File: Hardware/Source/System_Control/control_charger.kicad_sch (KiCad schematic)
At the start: 22 parts, among them Q21 LN2302LT1G, Q22 SQJ211ELP-T1_GE3, Q23 SQJ211ELP-T1_GE3, Q24 LN2302LT1G, U20 EL3H7, U21 EL3H7

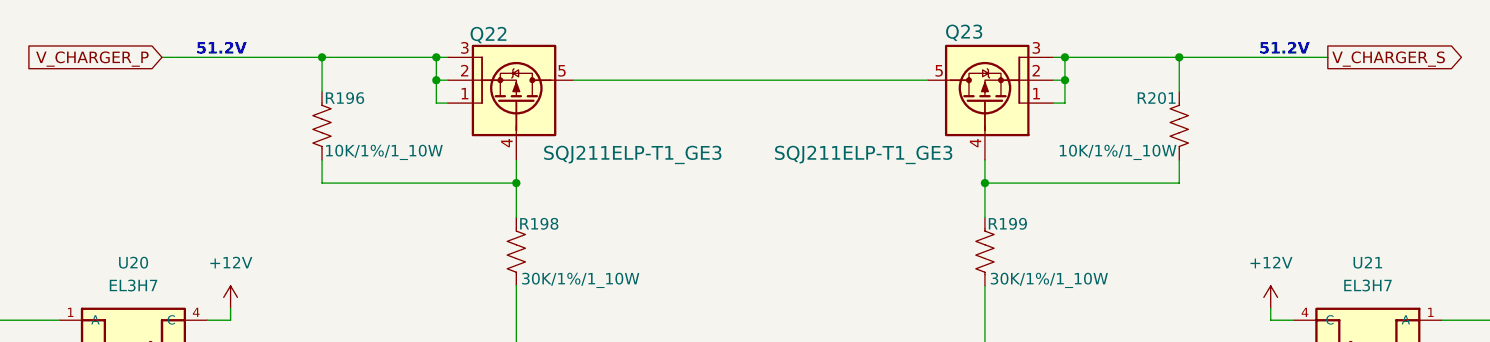
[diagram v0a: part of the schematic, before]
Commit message: schematic: update connector charger board F4
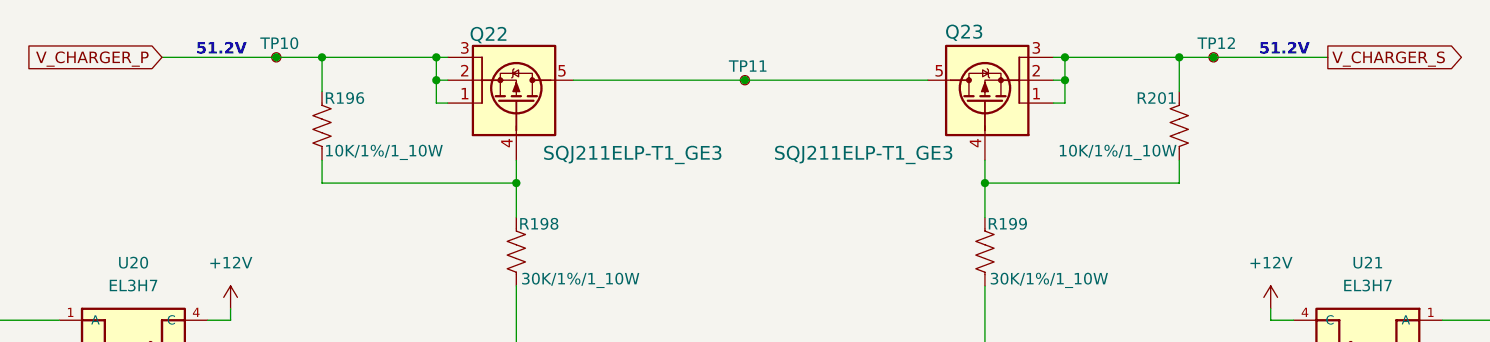
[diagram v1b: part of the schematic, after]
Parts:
- added TP10, TP11, TP12: TestPoint_Small, TestPoint:TestPoint_Pad_D1.0mm, symbol Connector:TestPoint_Small
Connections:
- net V_CHARGER_P: now also TP10.1
- net V_CHARGER_S: now also TP12.1
- net at Q22.5 (D), Q23.5 (D): now also TP11.1

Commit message: pcb,lib,sche: PFC, lib: update pcb PFC, lib
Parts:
- renumbered C164 to C169, C165 to C170, C166 to C171, C167 to C172, D76 to D75, D77 to D76, R194 to R196, R195 to R197, R196 to R198, R197 to R199, R198 to R200, R199 to R201, R200 to R202, R201 to R203, R202 to R204, R203 to R205
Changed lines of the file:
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@@
 		(on_board yes)
 		(dnp no)
-		(property "Reference" "R194"
+		(property "Reference" "R196"
 			(at 53.594 91.948 0)
 			(effects
@@
 			(project "System_Control"
 				(path "/85c53e8c-0403-413d-b6c5-0718d4365b1f/dcdba039-ea40-479a-8e78-13cd4769be17"
-					(reference "R194")
+					(reference "R196")
 					(unit 1)
 				)
@@
 		(on_board yes)
 		(dnp no)
-		(property "Reference" "R199"
+		(property "Reference" "R201"
 			(at 175.514 83.312 90)
 			(effects
@@
 			(project "System_Control"
 				(path "/85c53e8c-0403-413d-b6c5-0718d4365b1f/dcdba039-ea40-479a-8e78-13cd4769be17"
-					(reference "R199")
+					(reference "R201")
 					(unit 1)
 				)
@@
 		(on_board yes)
 		(dnp no)
-		(property "Reference" "R200"
+		(property "Reference" "R202"
 			(at 191.516 106.172 90)
 			(effects
@@
 			(project "System_Control"
 				(path "/85c53e8c-0403-413d-b6c5-0718d4365b1f/dcdba039-ea40-479a-8e78-13cd4769be17"
-					(reference "R200")
+					(reference "R202")
 					(unit 1)
 				)
@@
 		(on_board yes)
 		(dnp no)
-		(property "Reference" "C167"
+		(property "Reference" "C172"
 			(at 224.79 115.062 90)
 			(effects
@@
 			(project "System_Control"
 				(path "/85c53e8c-0403-413d-b6c5-0718d4365b1f/dcdba039-ea40-479a-8e78-13cd4769be17"
-					(reference "C167")
+					(reference "C172")
 					(unit 1)
 				)
@@
 		(on_board yes)
 		(dnp no)
-		(property "Reference" "C166"
+		(property "Reference" "C171"
 			(at 213.36 115.062 90)
 			(effects
@@
 			(project "System_Control"
 				(path "/85c53e8c-0403-413d-b6c5-0718d4365b1f/dcdba039-ea40-479a-8e78-13cd4769be17"
-					(reference "C166")
+					(reference "C171")
 					(unit 1)
 				)
@@
 		(on_board yes)
 		(dnp no)
-		(property "Reference" "C165"
+		(property "Reference" "C170"
 			(at 87.63 117.602 90)
 			(effects
@@
 			(project "System_Control"
 				(path "/85c53e8c-0403-413d-b6c5-0718d4365b1f/dcdba039-ea40-479a-8e78-13cd4769be17"
-					(reference "C165")
+					(reference "C170")
 					(unit 1)
 				)
@@
 		(on_board yes)
 		(dnp no)
-		(property "Reference" "R195"
+		(property "Reference" "R197"
 			(at 97.79 99.568 0)
 			(effects
@@
 			(project "System_Control"
 				(path "/85c53e8c-0403-413d-b6c5-0718d4365b1f/dcdba039-ea40-479a-8e78-13cd4769be17"
-					(reference "R195")
+					(reference "R197")
 					(unit 1)
 				)
@@
 		(on_board yes)
 		(dnp no)
-		(property "Reference" "R197"
+		(property "Reference" "R199"
 			(at 106.934 107.442 90)
 			(effects
@@
 			(project "System_Control"
 				(path "/85c53e8c-0403-413d-b6c5-0718d4365b1f/dcdba039-ea40-479a-8e78-13cd4769be17"
-					(reference "R197")
+					(reference "R199")
 					(unit 1)
 				)
@@
 		(on_board yes)
 		(dnp no)
-		(property "Reference" "R198"
+		(property "Reference" "R200"
 			(at 123.444 83.312 90)
 			(effects
@@
 			(project ""
 				(path "/85c53e8c-0403-413d-b6c5-0718d4365b1f/dcdba039-ea40-479a-8e78-13cd4769be17"
-					(reference "R198")
+					(reference "R200")
 					(unit 1)
 				)
@@
 		(on_board yes)
 		(dnp no)
-		(property "Reference" "C164"
+		(property "Reference" "C169"
 			(at 76.2 117.602 90)
 			(effects
@@
 			(project "System_Control"
 				(path "/85c53e8c-0403-413d-b6c5-0718d4365b1f/dcdba039-ea40-479a-8e78-13cd4769be17"
-					(reference "C164")
+					(reference "C169")
 					(unit 1)
 				)
@@
 		(on_board yes)
 		(dnp no)
-		(property "Reference" "D77"
+		(property "Reference" "D76"
 			(at 238.76 99.06 0)
 			(effects
@@
 			(project "System_Control"
 				(path "/85c53e8c-0403-413d-b6c5-0718d4365b1f/dcdba039-ea40-479a-8e78-13cd4769be17"
-					(reference "D77")
+					(reference "D76")
 					(unit 1)
 				)
@@
 		(on_board yes)
 		(dnp no)
-		(property "Reference" "R202"
+		(property "Reference" "R204"
 			(at 200.66 99.568 0)
 			(effects
@@
 			(project "System_Control"
 				(path "/85c53e8c-0403-413d-b6c5-0718d4365b1f/dcdba039-ea40-479a-8e78-13cd4769be17"
-					(reference "R202")
+					(reference "R204")
 					(unit 1)
 				)
@@
 		(on_board yes)
 		(dnp no)
-		(property "Reference" "R203"
+		(property "Reference" "R205"
 			(at 238.506 91.948 0)
 			(effects
@@
 			(project "System_Control"
 				(path "/85c53e8c-0403-413d-b6c5-0718d4365b1f/dcdba039-ea40-479a-8e78-13cd4769be17"
-					(reference "R203")
+					(reference "R205")
 					(unit 1)
 				)
@@
 		(on_board yes)
 		(dnp no)
-		(property "Reference" "D76"
+		(property "Reference" "D75"
 			(at 53.34 99.06 0)
 			(effects
@@
 			(project "System_Control"
 				(path "/85c53e8c-0403-413d-b6c5-0718d4365b1f/dcdba039-ea40-479a-8e78-13cd4769be17"
-					(reference "D76")
+					(reference "D75")
 					(unit 1)
 				)
@@
 		(on_board yes)
 		(dnp no)
-		(property "Reference" "R201"
+		(property "Reference" "R203"
 			(at 196.596 69.342 90)
 			(effects
@@
 			(project "System_Control"
 				(path "/85c53e8c-0403-413d-b6c5-0718d4365b1f/dcdba039-ea40-479a-8e78-13cd4769be17"
-					(reference "R201")
+					(reference "R203")
 					(unit 1)
 				)
@@
 		(on_board yes)
 		(dnp no)
-		(property "Reference" "R196"
+		(property "Reference" "R198"
 			(at 101.854 69.342 90)
 			(effects
@@
 			(project "System_Control"
 				(path "/85c53e8c-0403-413d-b6c5-0718d4365b1f/dcdba039-ea40-479a-8e78-13cd4769be17"
-					(reference "R196")
-					(unit 1)
-				)
+					(reference "R198")
+					(unit 1)
+				)

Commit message: pull
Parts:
- removed C169, C171: 10uF/16V, charge_battery_footprint_lib:Ceramic_Cap_0603, symbol charge_battery_sym_lib:Ceramic_Cap_SMD_10uF_16V
- removed C170, C172: 100nF/16V, charge_battery_footprint_lib:Ceramic_Cap_0603, symbol charge_battery_sym_lib:Ceramic_Cap_SMD_100nF_16V
- removed D75, D76: LED_0805, charge_battery_footprint_lib:LED_0805, symbol charge_battery_sym_lib:LED_0805
- removed Q21, Q24: LN2302LT1G, charge_battery_footprint_lib:SOT23, symbol charge_battery_sym_lib:LN2302LT1G
- removed R196, R205: 220/1%/1_10W, charge_battery_footprint_lib:Res_0603, symbol charge_battery_sym_lib:Res_220_0603_1%
- removed U20, U21: EL3H7, charge_battery_footprint_lib:SOIC_TA-VG, symbol charge_battery_sym_lib:EL3H7
- added Q21, Q24: MMBT2222A, charge_battery_footprint_lib:SOT23, symbol charge_battery_sym_lib:MMBT2222A
- renumbered R197 to R194, R198 to R195, R199 to R196, R200 to R197, R201 to R198, R202 to R199, R203 to R200, R204 to R201, TP11 to TP10, TP12 to TP11, TP10 to TP9
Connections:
- net CHARGE: now also R194.1
- net DISCHARGE: now also R201.2
- net GNDD: now also Q21.2 (E), Q24.2 (E)
- net at R194.2, R196.2: now also Q21.1 (B)
- net at R197.1: now also Q21.3 (C)
- net at R198.1: now also Q24.3 (C)
- net at R199.2, R201.1: now also Q24.1 (B)

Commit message: check
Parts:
- removed TP11, TP9: TestPoint_Small, TestPoint:TestPoint_Pad_D1.0mm, symbol Connector:TestPoint_Small
- renumbered R194 to R192, R195 to R193, R196 to R194, R197 to R195, R198 to R196, R199 to R197, R200 to R198, R201 to R199, TP10 to TP9
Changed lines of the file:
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@@
-	)
-	(junction
-		(at 200.66 64.77)
-		(diameter 0)
-		(color 0 0 0 0)
 	)
 	(junction
@@
 		(color 0 0 0 0)
 	)
-	(junction
-		(at 96.52 64.77)
-		(diameter 0)
-		(color 0 0 0 0)
-	)
 	(wire
 		(pts
@@
 	(wire
 		(pts
-			(xy 200.66 64.77) (xy 213.36 64.77)
+			(xy 196.85 64.77) (xy 213.36 64.77)
 		)
 		(stroke
@@
 	(wire
 		(pts
-			(xy 96.52 64.77) (xy 101.6 64.77)
-		)
-		(stroke
-			(width 0)
-			(type default)
-		)
-	)
-	(wire
-		(pts
-			(xy 83.82 64.77) (xy 96.52 64.77)
+			(xy 83.82 64.77) (xy 101.6 64.77)
 		)
 		(stroke
@@
 		(pts
 			(xy 106.68 116.84) (xy 106.68 114.3)
-		)
-		(stroke
-			(width 0)
-			(type default)
-		)
-	)
-	(wire
-		(pts
-			(xy 196.85 64.77) (xy 200.66 64.77)
 		)
 		(stroke
@@
 		(dnp no)
 		(fields_autoplaced yes)
-		(property "Reference" "#PWR0252"
+		(property "Reference" "#PWR0253"
 			(at 123.19 124.46 0)
 			(effects
@@
 			(project "System_Control"
 				(path "/85c53e8c-0403-413d-b6c5-0718d4365b1f/dcdba039-ea40-479a-8e78-13cd4769be17"
-					(reference "#PWR0252")
+					(reference "#PWR0253")
 					(unit 1)
 				)
@@
 		(on_board yes)
 		(dnp no)
-		(property "Reference" "R198"
+		(property "Reference" "R196"
 			(at 175.514 83.312 90)
 			(effects
@@
 			(project "System_Control"
 				(path "/85c53e8c-0403-413d-b6c5-0718d4365b1f/dcdba039-ea40-479a-8e78-13cd4769be17"
-					(reference "R198")
+					(reference "R196")
 					(unit 1)
 				)
@@
 		(on_board yes)
 		(dnp no)
-		(property "Reference" "R199"
+		(property "Reference" "R197"
 			(at 191.516 106.172 90)
 			(effects
@@
 			(project "System_Control"
 				(path "/85c53e8c-0403-413d-b6c5-0718d4365b1f/dcdba039-ea40-479a-8e78-13cd4769be17"
-					(reference "R199")
+					(reference "R197")
 					(unit 1)
 				)
@@
 	)
 	(symbol
-		(lib_id "Connector:TestPoint_Small")
-		(at 96.52 64.77 0)
-		(unit 1)
-		(exclude_from_sim no)
-		(in_bom yes)
-		(on_board yes)
-		(dnp no)
-		(property "Reference" "TP9"
-			(at 94.742 63.246 0)
-			(effects
-				(font
-					(size 1.27 1.27)
-				)
-				(justify left)
-			)
-		)
-		(property "Value" "TestPoint_Small"
-			(at 97.79 66.0399 0)
-			(effects
-				(font
-					(size 1.27 1.27)
-				)
-				(justify left)
-				(hide yes)
-			)
-		)
-		(property "Footprint" "TestPoint:TestPoint_Pad_D1.0mm"
-			(at 101.6 64.77 0)
-			(effects
-				(font
-					(size 1.27 1.27)
-				)
-				(hide yes)
-			)
-		)
-		(property "Datasheet" "~"
-			(at 101.6 64.77 0)
-			(effects
-				(font
-					(size 1.27 1.27)
-				)
-				(hide yes)
-			)
-		)
-		(property "Description" "test point"
-			(at 96.52 64.77 0)
-			(effects
-				(font
-					(size 1.27 1.27)
-				)
-				(hide yes)
-			)
-		)
-		(pin "1"
-		)
-		(instances
-			(project "System_Control"
-				(path "/85c53e8c-0403-413d-b6c5-0718d4365b1f/dcdba039-ea40-479a-8e78-13cd4769be17"
-					(reference "TP9")
-					(unit 1)
-				)
-			)
-		)
-	)
-	(symbol
 		(lib_id "charge_battery_sym_lib:Res_1K_0603_1%")
 		(at 93.98 101.6 0)
@@
 		(on_board yes)
 		(dnp no)
-		(property "Reference" "R194"
+		(property "Reference" "R192"
 			(at 97.79 99.568 0)
 			(effects
@@
 			(project "System_Control"
 				(path "/85c53e8c-0403-413d-b6c5-0718d4365b1f/dcdba039-ea40-479a-8e78-13cd4769be17"
-					(reference "R194")
+					(reference "R192")
 					(unit 1)
 				)
@@
 		(on_board yes)
 		(dnp no)
-		(property "Reference" "R196"
+		(property "Reference" "R194"
 			(at 106.934 107.442 90)
 			(effects
@@
 			(project "System_Control"
 				(path "/85c53e8c-0403-413d-b6c5-0718d4365b1f/dcdba039-ea40-479a-8e78-13cd4769be17"
-					(reference "R196")
+					(reference "R194")
 					(unit 1)
 				)
@@
 		(on_board yes)
 		(dnp no)
-		(property "Reference" "R197"
+		(property "Reference" "R195"
 			(at 123.444 83.312 90)
 			(effects
@@
 			(project ""
 				(path "/85c53e8c-0403-413d-b6c5-0718d4365b1f/dcdba039-ea40-479a-8e78-13cd4769be17"
-					(reference "R197")
+					(reference "R195")
 					(unit 1)
 				)
@@
 		(on_board yes)
 		(dnp no)
-		(property "Reference" "TP10"
+		(property "Reference" "TP9"
 			(at 146.812 65.786 0)
 			(effects
@@
 			(project "System_Control"
 				(path "/85c53e8c-0403-413d-b6c5-0718d4365b1f/dcdba039-ea40-479a-8e78-13cd4769be17"
-					(reference "TP10")
+					(reference "TP9")
 					(unit 1)
 				)
@@
 		(on_board yes)
 		(dnp no)
-		(property "Reference" "R201"
+		(property "Reference" "R199"
 			(at 200.66 99.568 0)
 			(effects
@@
 			(project "System_Control"
 				(path "/85c53e8c-0403-413d-b6c5-0718d4365b1f/dcdba039-ea40-479a-8e78-13cd4769be17"
-					(reference "R201")
+					(reference "R199")
 					(unit 1)
 				)
@@
 		(dnp no)
 		(fields_autoplaced yes)
-		(property "Reference" "#PWR0253"
+		(property "Reference" "#PWR0254"
 			(at 175.26 124.46 0)
 			(effects
@@
 			(project "System_Control"
 				(path "/85c53e8c-0403-413d-b6c5-0718d4365b1f/dcdba039-ea40-479a-8e78-13cd4769be17"
-					(reference "#PWR0253")
-					(unit 1)
-				)
-			)
-		)
-	)
-	(symbol
-		(lib_id "Connector:TestPoint_Small")
-		(at 200.66 64.77 0)
-		(unit 1)
-		(exclude_from_sim no)
-		(in_bom yes)
-		(on_board yes)
-		(dnp no)
-		(property "Reference" "TP11"
-			(at 198.882 63.246 0)
-			(effects
-				(font
-					(size 1.27 1.27)
-				)
-				(justify left)
-			)
-		)
-		(property "Value" "TestPoint_Small"
-			(at 201.93 66.0399 0)
-			(effects
-				(font
-					(size 1.27 1.27)
-				)
-				(justify left)
-				(hide yes)
-			)
-		)
-		(property "Footprint" "TestPoint:TestPoint_Pad_D1.0mm"
-			(at 205.74 64.77 0)
-			(effects
-				(font
-					(size 1.27 1.27)
-				)
-				(hide yes)
-			)
-		)
-		(property "Datasheet" "~"
-			(at 205.74 64.77 0)
-			(effects
-				(font
-					(size 1.27 1.27)
-				)
-				(hide yes)
-			)
-		)
-		(property "Description" "test point"
-			(at 200.66 64.77 0)
-			(effects
-				(font
-					(size 1.27 1.27)
-				)
-				(hide yes)
-			)
-		)
-		(pin "1"
-		)
-		(instances
-			(project "System_Control"
-				(path "/85c53e8c-0403-413d-b6c5-0718d4365b1f/dcdba039-ea40-479a-8e78-13cd4769be17"
-					(reference "TP11")
+					(reference "#PWR0254")
 					(unit 1)
 				)
@@
 		(on_board yes)
 		(dnp no)
-		(property "Reference" "R200"
+		(property "Reference" "R198"
 			(at 196.596 69.342 90)
 			(effects
@@
 			(project "System_Control"
 				(path "/85c53e8c-0403-413d-b6c5-0718d4365b1f/dcdba039-ea40-479a-8e78-13cd4769be17"
-					(reference "R200")
+					(reference "R198")
 					(unit 1)
 				)
@@
 		(on_board yes)
 		(dnp no)
-		(property "Reference" "R195"
+		(property "Reference" "R193"
 			(at 101.854 69.342 90)
 			(effects
@@
 			(project "System_Control"
 				(path "/85c53e8c-0403-413d-b6c5-0718d4365b1f/dcdba039-ea40-479a-8e78-13cd4769be17"
-					(reference "R195")
+					(reference "R193")
 					(unit 1)
 				)

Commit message: check
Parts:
- renumbered R192 to R193, R193 to R194, R194 to R195, R195 to R196, R196 to R197, R197 to R198, R198 to R199, R199 to R200, TP9 to TP4
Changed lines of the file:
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@@
 		(dnp no)
 		(fields_autoplaced yes)
-		(property "Reference" "#PWR0253"
+		(property "Reference" "#PWR0251"
 			(at 123.19 124.46 0)
 			(effects
@@
 			(project "System_Control"
 				(path "/85c53e8c-0403-413d-b6c5-0718d4365b1f/dcdba039-ea40-479a-8e78-13cd4769be17"
-					(reference "#PWR0253")
+					(reference "#PWR0251")
 					(unit 1)
 				)
@@
 		(on_board yes)
 		(dnp no)
-		(property "Reference" "R196"
+		(property "Reference" "R197"
 			(at 175.514 83.312 90)
 			(effects
@@
 			(project "System_Control"
 				(path "/85c53e8c-0403-413d-b6c5-0718d4365b1f/dcdba039-ea40-479a-8e78-13cd4769be17"
-					(reference "R196")
+					(reference "R197")
 					(unit 1)
 				)
@@
 		(on_board yes)
 		(dnp no)
-		(property "Reference" "R197"
+		(property "Reference" "R198"
 			(at 191.516 106.172 90)
 			(effects
@@
 			(project "System_Control"
 				(path "/85c53e8c-0403-413d-b6c5-0718d4365b1f/dcdba039-ea40-479a-8e78-13cd4769be17"
-					(reference "R197")
+					(reference "R198")
 					(unit 1)
 				)
@@
 		(on_board yes)
 		(dnp no)
-		(property "Reference" "R192"
+		(property "Reference" "R193"
 			(at 97.79 99.568 0)
 			(effects
@@
 			(project "System_Control"
 				(path "/85c53e8c-0403-413d-b6c5-0718d4365b1f/dcdba039-ea40-479a-8e78-13cd4769be17"
-					(reference "R192")
+					(reference "R193")
 					(unit 1)
 				)
@@
 		(on_board yes)
 		(dnp no)
-		(property "Reference" "R194"
+		(property "Reference" "R195"
 			(at 106.934 107.442 90)
 			(effects
@@
 			(project "System_Control"
 				(path "/85c53e8c-0403-413d-b6c5-0718d4365b1f/dcdba039-ea40-479a-8e78-13cd4769be17"
-					(reference "R194")
+					(reference "R195")
 					(unit 1)
 				)
@@
 		(on_board yes)
 		(dnp no)
-		(property "Reference" "R195"
+		(property "Reference" "R196"
 			(at 123.444 83.312 90)
 			(effects
@@
 			(project ""
 				(path "/85c53e8c-0403-413d-b6c5-0718d4365b1f/dcdba039-ea40-479a-8e78-13cd4769be17"
-					(reference "R195")
+					(reference "R196")
 					(unit 1)
 				)
@@
 		(on_board yes)
 		(dnp no)
-		(property "Reference" "TP9"
+		(property "Reference" "TP4"
 			(at 146.812 65.786 0)
 			(effects
@@
 			(project "System_Control"
 				(path "/85c53e8c-0403-413d-b6c5-0718d4365b1f/dcdba039-ea40-479a-8e78-13cd4769be17"
-					(reference "TP9")
+					(reference "TP4")
 					(unit 1)
 				)
@@
 		(on_board yes)
 		(dnp no)
-		(property "Reference" "R199"
+		(property "Reference" "R200"
 			(at 200.66 99.568 0)
 			(effects
@@
 			(project "System_Control"
 				(path "/85c53e8c-0403-413d-b6c5-0718d4365b1f/dcdba039-ea40-479a-8e78-13cd4769be17"
-					(reference "R199")
+					(reference "R200")
 					(unit 1)
 				)
@@
 		(dnp no)
 		(fields_autoplaced yes)
-		(property "Reference" "#PWR0254"
+		(property "Reference" "#PWR0252"
 			(at 175.26 124.46 0)
 			(effects
@@
 			(project "System_Control"
 				(path "/85c53e8c-0403-413d-b6c5-0718d4365b1f/dcdba039-ea40-479a-8e78-13cd4769be17"
-					(reference "#PWR0254")
+					(reference "#PWR0252")
 					(unit 1)
 				)
@@
 		(on_board yes)
 		(dnp no)
-		(property "Reference" "R198"
+		(property "Reference" "R199"
 			(at 196.596 69.342 90)
 			(effects
@@
 			(project "System_Control"
 				(path "/85c53e8c-0403-413d-b6c5-0718d4365b1f/dcdba039-ea40-479a-8e78-13cd4769be17"
-					(reference "R198")
+					(reference "R199")
 					(unit 1)
 				)
@@
 		(on_board yes)
 		(dnp no)
-		(property "Reference" "R193"
+		(property "Reference" "R194"
 			(at 101.854 69.342 90)
 			(effects
@@
 			(project "System_Control"
 				(path "/85c53e8c-0403-413d-b6c5-0718d4365b1f/dcdba039-ea40-479a-8e78-13cd4769be17"
-					(reference "R193")
-					(unit 1)
-				)
+					(reference "R194")
+					(unit 1)
+				)
